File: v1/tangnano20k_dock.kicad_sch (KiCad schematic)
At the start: 41 parts, among them J1 Mini-DIN-6, J2 2x20 Pin Female, J3 Conn_01x03_Male, J4 Conn_01x20, J5 Conn_01x02, J6 RCA, J7 FCR684205T, J8 AudioJack3, U1 TXS0104E, U2 TangNano20K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

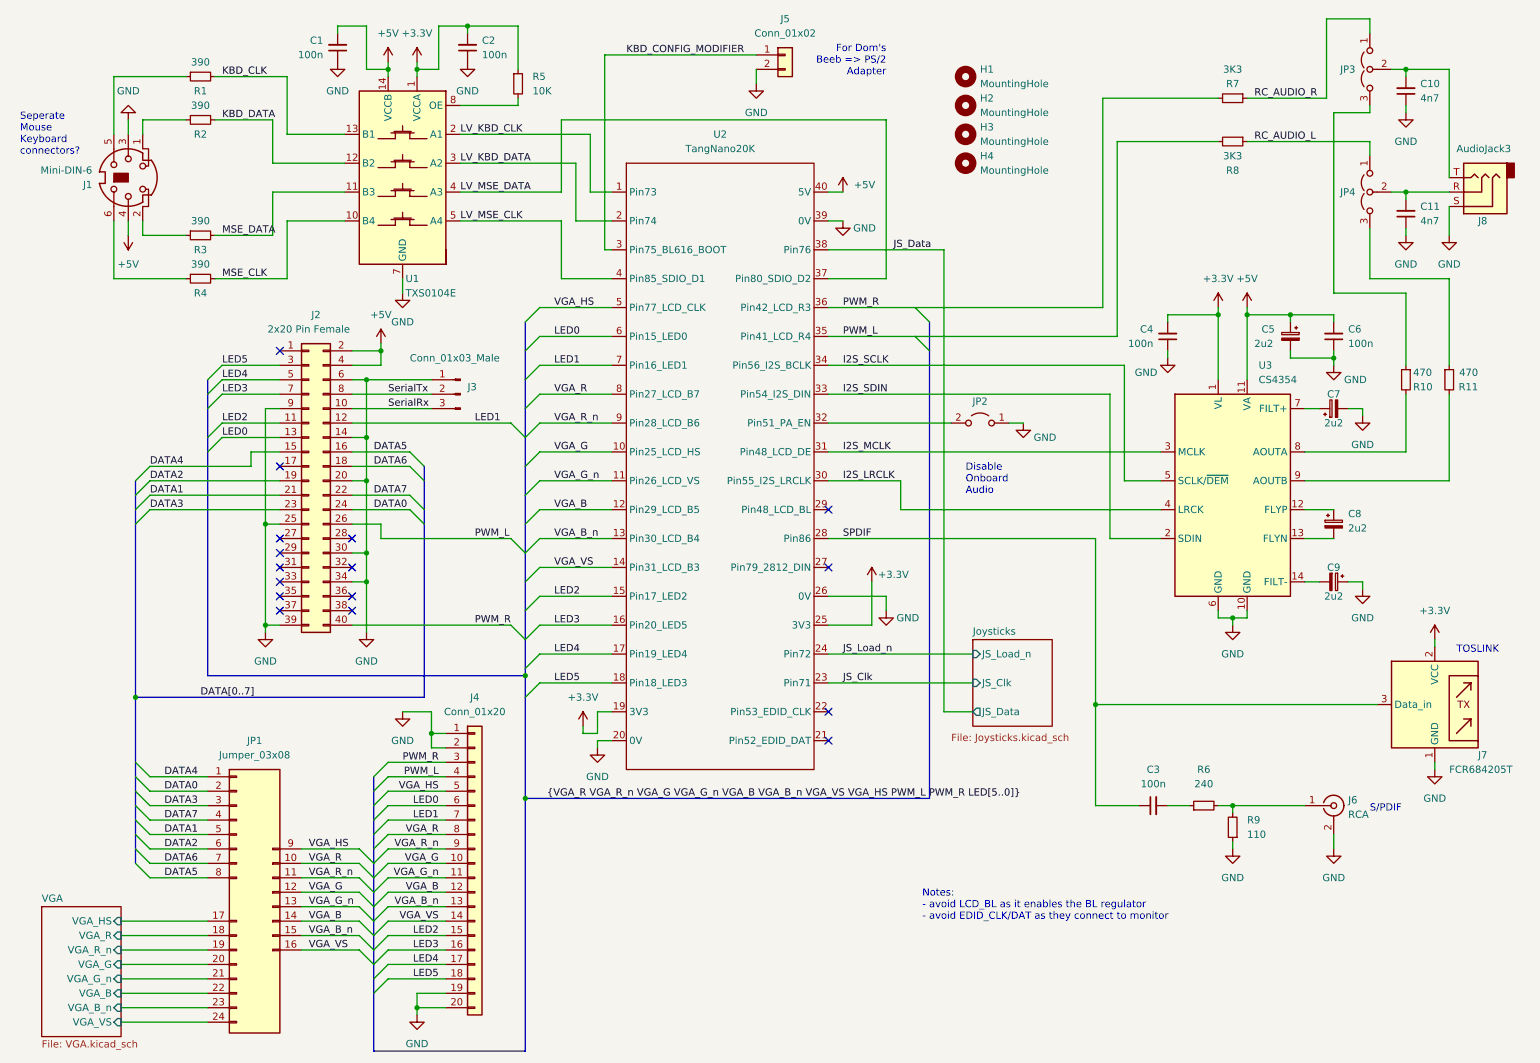
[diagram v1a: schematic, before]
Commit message: Silk-screen and swap PWM L/R labels
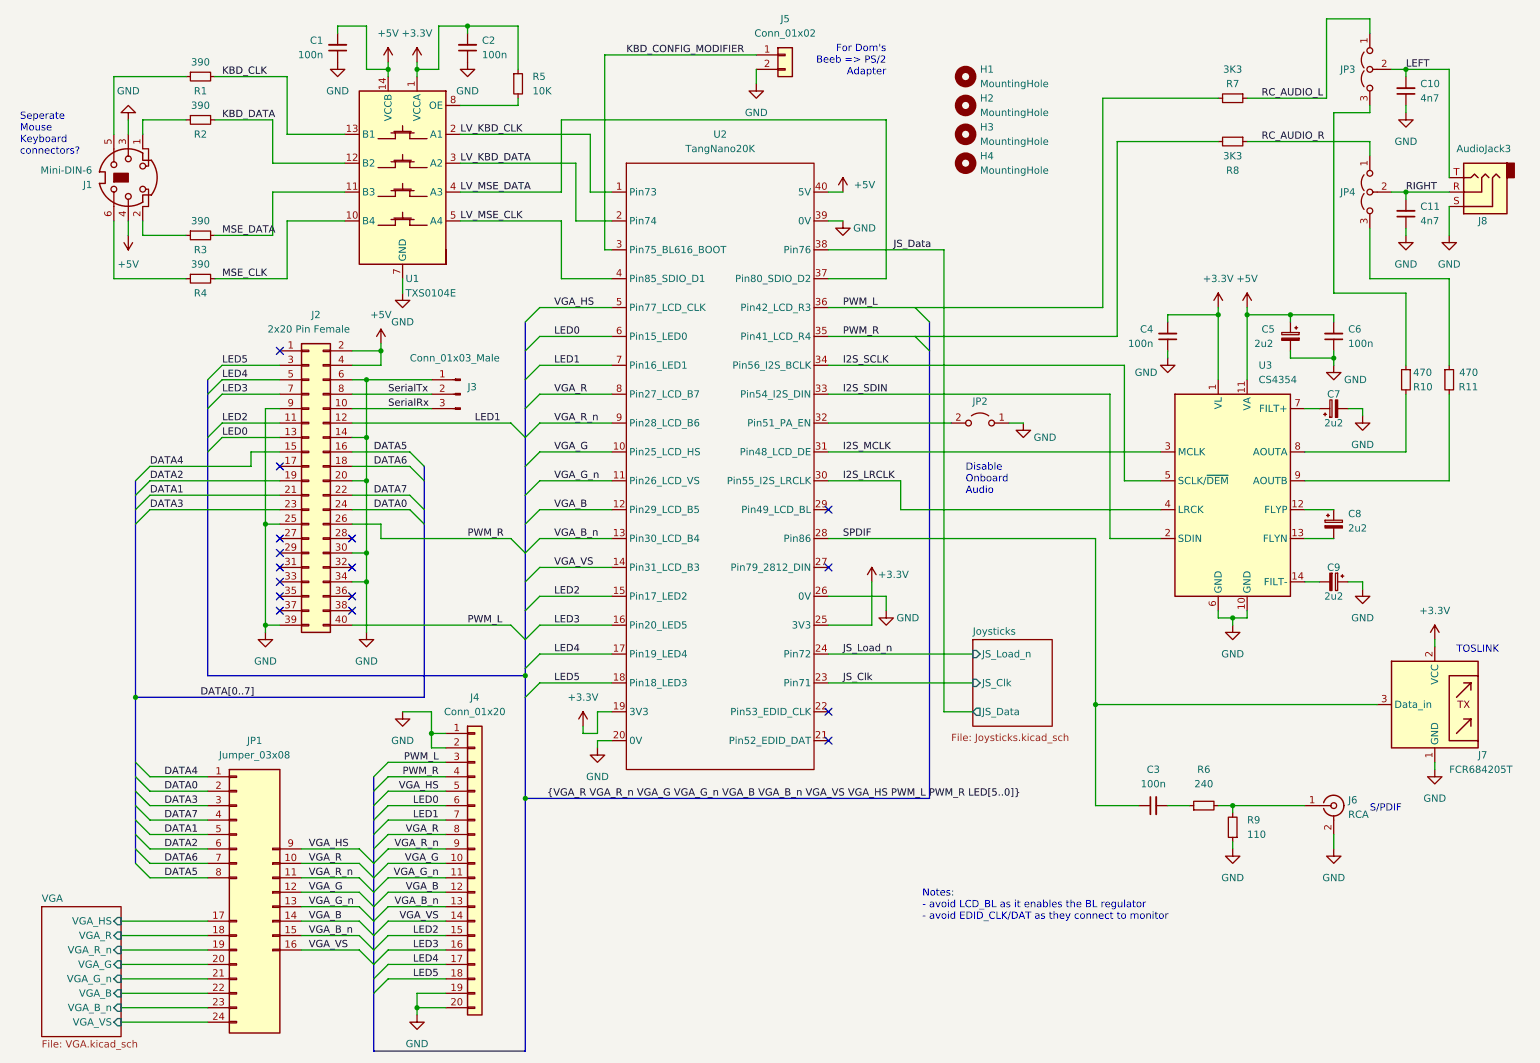
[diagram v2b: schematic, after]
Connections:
- net PWM_L: now also J2.40 (Pin_40), J4.3 (Pin_3), R7.2, U2.36 (Pin42_LCD_R3); no longer J2.26 (Pin_26), J4.4 (Pin_4), R8.2, U2.35 (Pin41_LCD_R4)
- net PWM_R: now also J2.26 (Pin_26), J4.4 (Pin_4), R8.2, U2.35 (Pin41_LCD_R4); no longer J2.40 (Pin_40), J4.3 (Pin_3), R7.2, U2.36 (Pin42_LCD_R3)
- net RC_AUDIO_L: now also JP3.1 (A), R7.1; no longer JP4.1 (A), R8.1
- net RC_AUDIO_R: now also JP4.1 (A), R8.1; no longer JP3.1 (A), R7.1
- net RIGHT: now reaches C11.2, J8.R, JP4.2 (C)
- net LEFT: now reaches C10.2, J8.T, JP3.2 (C)
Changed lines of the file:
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@@
     (effects (font (size 1.27 1.27)) (justify left bottom))
   )
-  (label "PWM_R" (at 92.71 144.78 180)
+  (label "PWM_R" (at 92.71 147.32 180)
     (effects (font (size 1.27 1.27)) (justify right bottom))
   )
@@
     (effects (font (size 1.27 1.27)) (justify left bottom))
   )
-  (label "PWM_L" (at 163.83 69.85 0)
+  (label "PWM_L" (at 163.83 64.77 0)
     (effects (font (size 1.27 1.27)) (justify left bottom))
   )
@@
     (effects (font (size 1.27 1.27)) (justify left bottom))
   )
+  (label "RIGHT" (at 262.89 44.45 0)
+    (effects (font (size 1.27 1.27)) (justify left bottom))
+  )
   (label "DATA1" (at 41.91 97.79 0)
     (effects (font (size 1.27 1.27)) (justify left bottom))
@@
     (effects (font (size 1.27 1.27)) (justify left bottom))
   )
+  (label "LEFT" (at 262.89 22.86 0)
+    (effects (font (size 1.27 1.27)) (justify left bottom))
+  )
   (label "VGA_VS" (at 92.71 172.72 180)
     (effects (font (size 1.27 1.27)) (justify right bottom))
@@
     (effects (font (size 1.27 1.27)) (justify left bottom))
   )
-  (label "PWM_R" (at 163.83 64.77 0)
+  (label "PWM_R" (at 163.83 69.85 0)
     (effects (font (size 1.27 1.27)) (justify left bottom))
   )
@@
     (effects (font (size 1.27 1.27)) (justify left bottom))
   )
-  (label "PWM_L" (at 99.06 105.41 0)
-    (effects (font (size 1.27 1.27)) (justify left bottom))
-  )
-  (label "RC_AUDIO_R" (at 236.22 27.94 0)
+  (label "PWM_L" (at 97.79 120.65 0)
+    (effects (font (size 1.27 1.27)) (justify left bottom))
+  )
+  (label "RC_AUDIO_R" (at 237.49 35.56 0)
     (effects (font (size 1.27 1.27)) (justify left bottom))
   )
@@
     (effects (font (size 1.27 1.27)) (justify left bottom))
   )
-  (label "PWM_R" (at 99.06 120.65 0)
-    (effects (font (size 1.27 1.27)) (justify left bottom))
-  )
-  (label "PWM_L" (at 92.71 147.32 180)
-    (effects (font (size 1.27 1.27)) (justify right bottom))
-  )
-  (label "RC_AUDIO_L" (at 236.22 35.56 0)
-    (effects (font (size 1.27 1.27)) (justify left bottom))
-  )
+  (label "PWM_R" (at 97.79 105.41 0)
+    (effects (font (size 1.27 1.27)) (justify left bottom))
+  )
+  (label "PWM_L" (at 92.71 144.78 180)
+    (effects (font (size 1.27 1.27)) (justify right bottom))
+  )
+  (label "RC_AUDIO_L" (at 237.49 27.94 0)
+    (effects (font (size 1.27 1.27)) (justify left bottom))
+  )

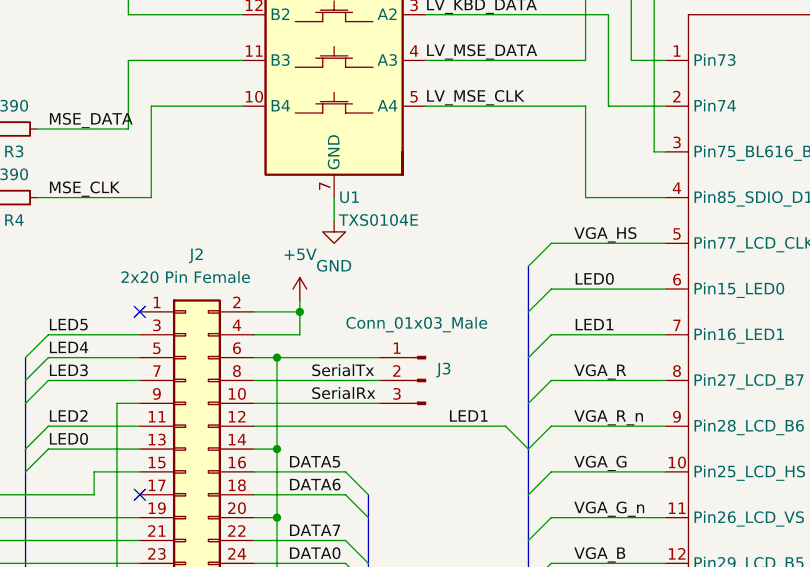
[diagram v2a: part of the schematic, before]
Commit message: Added jumpers for Pi and Joystick power
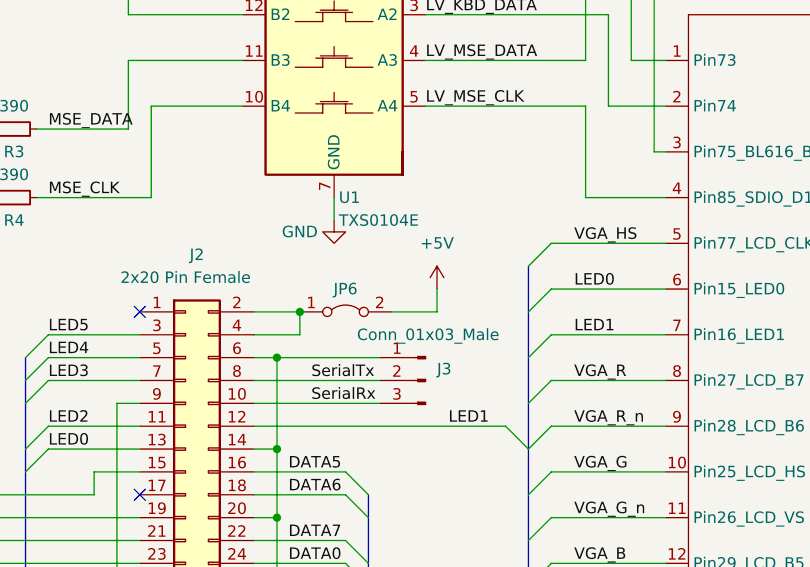
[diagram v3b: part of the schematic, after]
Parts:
- added JP6: Jumper_2_Bridged, Connector_PinHeader_2.54mm:PinHeader_1x02_P2.54mm_Vertical, symbol Jumper:Jumper_2_Bridged
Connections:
- net +5V: now also JP6.2 (B); no longer J2.2 (Pin_2), J2.4 (Pin_4)
- new net: J2.2 (Pin_2), J2.4 (Pin_4), JP6.1 (A)
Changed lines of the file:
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@@
   (junction (at 232.41 152.4) (diameter 0) (color 0 0 0 0)
   )
-  (junction (at 82.55 72.39) (diameter 0) (color 0 0 0 0)
-  )
   (junction (at 88.9 22.86) (diameter 0) (color 0 0 0 0)
   )
@@
   (junction (at 62.23 120.65) (diameter 0) (color 0 0 0 0)
   )
+  (junction (at 82.55 72.39) (diameter 0) (color 0 0 0 0)
+  )
   (junction (at 80.01 107.95) (diameter 0) (color 0 0 0 0)
   )
@@
     (stroke (width 0) (type default) (color 0 0 0 0))
   )
+  (wire (pts (xy 92.71 72.39) (xy 97.79 72.39))
+    (stroke (width 0) (type default) (color 0 0 0 0))
+  )
   (wire (pts (xy 234.95 66.04) (xy 234.95 77.47))
     (stroke (width 0) (type default) (color 0 0 0 0))
@@
     (stroke (width 0) (type default) (color 0 0 0 0))
   )
-  (wire (pts (xy 82.55 71.12) (xy 82.55 72.39))
-    (stroke (width 0) (type default) (color 0 0 0 0))
-  )
   (wire (pts (xy 118.11 139.7) (xy 120.65 139.7))
     (stroke (width 0) (type default) (color 0 0 0 0))
@@
     (stroke (width 0) (type default) (color 0 0 0 0))
   )
+  (wire (pts (xy 97.79 72.39) (xy 97.79 69.85))
+    (stroke (width 0) (type default) (color 0 0 0 0))
+  )
   (wire (pts (xy 92.71 22.86) (xy 92.71 15.24))
     (stroke (width 0) (type default) (color 0 0 0 0))
@@
     (pin "1")
   )
-  (symbol (lib_id "power:+5V") (at 82.55 71.12 0) (unit 1)
+  (symbol (lib_id "power:+5V") (at 97.79 69.85 0) (unit 1)
     (in_bom yes) (on_board yes)
-    (property "Reference" "#PWR06" (id 0) (at 82.55 74.93 0)
+    (property "Reference" "#PWR06" (id 0) (at 97.79 73.66 0)
       (effects (font (size 1.27 1.27)) hide)
     )
-    (property "Value" "+5V" (id 1) (at 82.55 66.04 0))
-    (property "Footprint" "" (id 2) (at 82.55 71.12 0)
+    (property "Value" "+5V" (id 1) (at 97.79 64.77 0))
+    (property "Footprint" "" (id 2) (at 97.79 69.85 0)
       (effects (font (size 1.27 1.27)) hide)
     )
-    (property "Datasheet" "" (id 3) (at 82.55 71.12 0)
+    (property "Datasheet" "" (id 3) (at 97.79 69.85 0)
       (effects (font (size 1.27 1.27)) hide)
     )
@@
       (effects (font (size 1.27 1.27)) (justify right))
     )
-    (property "Value" "Conn_01x03_Male" (id 1) (at 87.63 73.66 0)
+    (property "Value" "Conn_01x03_Male" (id 1) (at 88.9 74.93 0)
       (effects (font (size 1.27 1.27)) (justify right))
     )
@@
     (pin "1")
   )
+  (symbol (lib_id "Jumper:Jumper_2_Bridged") (at 87.63 72.39 0) (unit 1)
+    (in_bom yes) (on_board yes)
+    (property "Reference" "JP6" (id 0) (at 87.63 69.85 0))
+    (property "Value" "Jumper_2_Bridged" (id 1) (at 87.63 68.58 0)
+      (effects (font (size 1.27 1.27)) hide)
+    )
+    (property "Footprint" "Connector_PinHeader_2.54mm:PinHeader_1x02_P2.54mm_Vertical" (id 2) (at 87.63 72.39 0)
+      (effects (font (size 1.27 1.27)) hide)
+    )
+    (property "Datasheet" "~" (id 3) (at 87.63 72.39 0)
+      (effects (font (size 1.27 1.27)) hide)
+    )
+    (pin "1")
+    (pin "2")
+  )
   (symbol (lib_id "Jumper:Jumper_2_Open") (at 187.96 85.09 0) (mirror y) (unit 1)
     (in_bom yes) (on_board yes) (fields_autoplaced)
@@
   )
   (symbol (lib_id "power:GND") (at 86.36 62.23 0) (unit 1)
-    (in_bom yes) (on_board yes) (fields_autoplaced)
+    (in_bom yes) (on_board yes)
     (property "Reference" "#PWR08" (id 0) (at 86.36 68.58 0)
       (effects (font (size 1.27 1.27)) hide)
     )
-    (property "Value" "GND" (id 1) (at 86.36 67.31 0))
+    (property "Value" "GND" (id 1) (at 82.55 63.5 0))
     (property "Footprint" "" (id 2) (at 86.36 62.23 0)
       (effects (font (size 1.27 1.27)) hide)
@@
       (reference "JP5") (unit 1) (value "Conn_02x06_Odd_Even") (footprint "Connector_PinHeader_2.54mm:PinHeader_2x06_P2.54mm_Vertical")
     )
+    (path "/ac0b1739-f020-4d4b-8ea2-11fa6e63adfe"
+      (reference "JP6") (unit 1) (value "Jumper_2_Bridged") (footprint "Connector_PinHeader_2.54mm:PinHeader_1x02_P2.54mm_Vertical")
+    )
+    (path "/0331ec4d-b3bf-4145-9efb-ad1204df77fa/73d69a5d-82f0-4701-b385-5a2b33a96fb2"
+      (reference "JP7") (unit 1) (value "Jumper_2_Open") (footprint "Connector_PinHeader_2.54mm:PinHeader_1x02_P2.54mm_Vertical")
+    )
+    (path "/0331ec4d-b3bf-4145-9efb-ad1204df77fa/352c909d-8a74-4643-b8e9-826cbce5baa4"
+      (reference "JP8") (unit 1) (value "Jumper_2_Open") (footprint "Connector_PinHeader_2.54mm:PinHeader_1x02_P2.54mm_Vertical")
+    )
     (path "/99dba36f-0791-4286-9889-5ed93bc1d54a/3561f704-3f01-4eeb-835c-843f68920e0a"

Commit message: Switched to Cliffe FC68131 Jack (matches CUI_SJ1-3523N footprint)
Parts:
- J8: footprint TangNano20k:Jack_3.5mm_Lumberg_1503_07_Horizontal -> TangNano20k:Jack_3.5mm_CUI_SJ1-3523N_Horizontal
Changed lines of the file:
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@@
       (effects (font (size 1.27 1.27)) (justify right))
     )
-    (property "Footprint" "TangNano20k:Jack_3.5mm_Lumberg_1503_07_Horizontal" (id 2) (at 275.59 44.45 0)
+    (property "Footprint" "TangNano20k:Jack_3.5mm_CUI_SJ1-3523N_Horizontal" (id 2) (at 275.59 44.45 0)
       (effects (font (size 1.27 1.27)) hide)
     )
@@
     )
     (path "/4877468b-ee74-43f7-a4dc-6a0ddb9f2b4d"
-      (reference "J8") (unit 1) (value "AudioJack3") (footprint "TangNano20k:Jack_3.5mm_Lumberg_1503_07_Horizontal")
+      (reference "J8") (unit 1) (value "AudioJack3") (footprint "TangNano20k:Jack_3.5mm_CUI_SJ1-3523N_Horizontal")
     )
     (path "/99dba36f-0791-4286-9889-5ed93bc1d54a/43d73b4f-c3a1-4d26-9e13-eae64fb1719d"

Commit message: Extend board to allow mounting holes for Raspberry Pi
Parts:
- J2: footprint Connector_PinSocket_2.54mm:PinSocket_2x20_P2.54mm_Vertical -> TangNano20k:Raspberry_Pi_Zero_Socketed_THT_FaceDown_MountingHoles
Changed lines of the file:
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@@
     (property "Reference" "J2" (id 0) (at 71.12 66.04 0))
     (property "Value" "2x20 Pin Female" (id 1) (at 69.85 68.58 0))
-    (property "Footprint" "Connector_PinSocket_2.54mm:PinSocket_2x20_P2.54mm_Vertical" (id 2) (at 69.85 95.25 0)
+    (property "Footprint" "TangNano20k:Raspberry_Pi_Zero_Socketed_THT_FaceDown_MountingHoles" (id 2) (at 69.85 95.25 0)
       (effects (font (size 1.27 1.27)) hide)
     )
@@
     )
     (path "/85beec70-e003-477e-bc44-e48b266bacd8"
-      (reference "J2") (unit 1) (value "2x20 Pin Female") (footprint "Connector_PinSocket_2.54mm:PinSocket_2x20_P2.54mm_Vertical")
+      (reference "J2") (unit 1) (value "2x20 Pin Female") (footprint "TangNano20k:Raspberry_Pi_Zero_Socketed_THT_FaceDown_MountingHoles")
     )
     (path "/7e3d36e3-8c4f-4d6a-a649-cbd6581978b4"

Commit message: Add clearance around mounting holes
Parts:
- H1, H2, H3, H4: footprint MountingHole:MountingHole_3.2mm_M3 -> TangNano20k:MountingHole_3.2mm_M3
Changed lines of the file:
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@@
       (effects (font (size 1.27 1.27)) (justify left))
     )
-    (property "Footprint" "MountingHole:MountingHole_3.2mm_M3" (id 2) (at 185.42 39.37 0)
+    (property "Footprint" "TangNano20k:MountingHole_3.2mm_M3" (id 2) (at 185.42 39.37 0)
       (effects (font (size 1.27 1.27)) hide)
     )
@@
       (effects (font (size 1.27 1.27)) (justify left))
     )
-    (property "Footprint" "MountingHole:MountingHole_3.2mm_M3" (id 2) (at 185.42 24.13 0)
+    (property "Footprint" "TangNano20k:MountingHole_3.2mm_M3" (id 2) (at 185.42 24.13 0)
       (effects (font (size 1.27 1.27)) hide)
     )
@@
       (effects (font (size 1.27 1.27)) (justify left))
     )
-    (property "Footprint" "MountingHole:MountingHole_3.2mm_M3" (id 2) (at 185.42 34.29 0)
+    (property "Footprint" "TangNano20k:MountingHole_3.2mm_M3" (id 2) (at 185.42 34.29 0)
       (effects (font (size 1.27 1.27)) hide)
     )
@@
       (effects (font (size 1.27 1.27)) (justify left))
     )
-    (property "Footprint" "MountingHole:MountingHole_3.2mm_M3" (id 2) (at 185.42 29.21 0)
+    (property "Footprint" "TangNano20k:MountingHole_3.2mm_M3" (id 2) (at 185.42 29.21 0)
       (effects (font (size 1.27 1.27)) hide)
     )
@@
     )
     (path "/3efa4c66-1bea-40a4-bda9-02b28c07af29"
-      (reference "H1") (unit 1) (value "MountingHole") (footprint "MountingHole:MountingHole_3.2mm_M3")
+      (reference "H1") (unit 1) (value "MountingHole") (footprint "TangNano20k:MountingHole_3.2mm_M3")
     )
     (path "/f95e5f0b-56a0-442b-9f1b-cce491951b72"
-      (reference "H2") (unit 1) (value "MountingHole") (footprint "MountingHole:MountingHole_3.2mm_M3")
+      (reference "H2") (unit 1) (value "MountingHole") (footprint "TangNano20k:MountingHole_3.2mm_M3")
     )
     (path "/820967dd-e818-4da1-bb9b-2a6bbdeea89d"
-      (reference "H3") (unit 1) (value "MountingHole") (footprint "MountingHole:MountingHole_3.2mm_M3")
+      (reference "H3") (unit 1) (value "MountingHole") (footprint "TangNano20k:MountingHole_3.2mm_M3")
     )
     (path "/2edda0e4-403b-45ec-b8d6-bae5fe9a549d"
-      (reference "H4") (unit 1) (value "MountingHole") (footprint "MountingHole:MountingHole_3.2mm_M3")
+      (reference "H4") (unit 1) (value "MountingHole") (footprint "TangNano20k:MountingHole_3.2mm_M3")
     )
     (path "/9becf180-126c-4cc1-ba0f-3c658ab540d4"
